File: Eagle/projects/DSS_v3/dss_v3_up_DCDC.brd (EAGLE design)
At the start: 50 x 83 mm, 58 parts, among them IC1 MC34063AD, IC2 Atmega8a, IC3 TL431, J1 12-24V, SW1 EC12E_SW, T1 BC846, X1 PS2

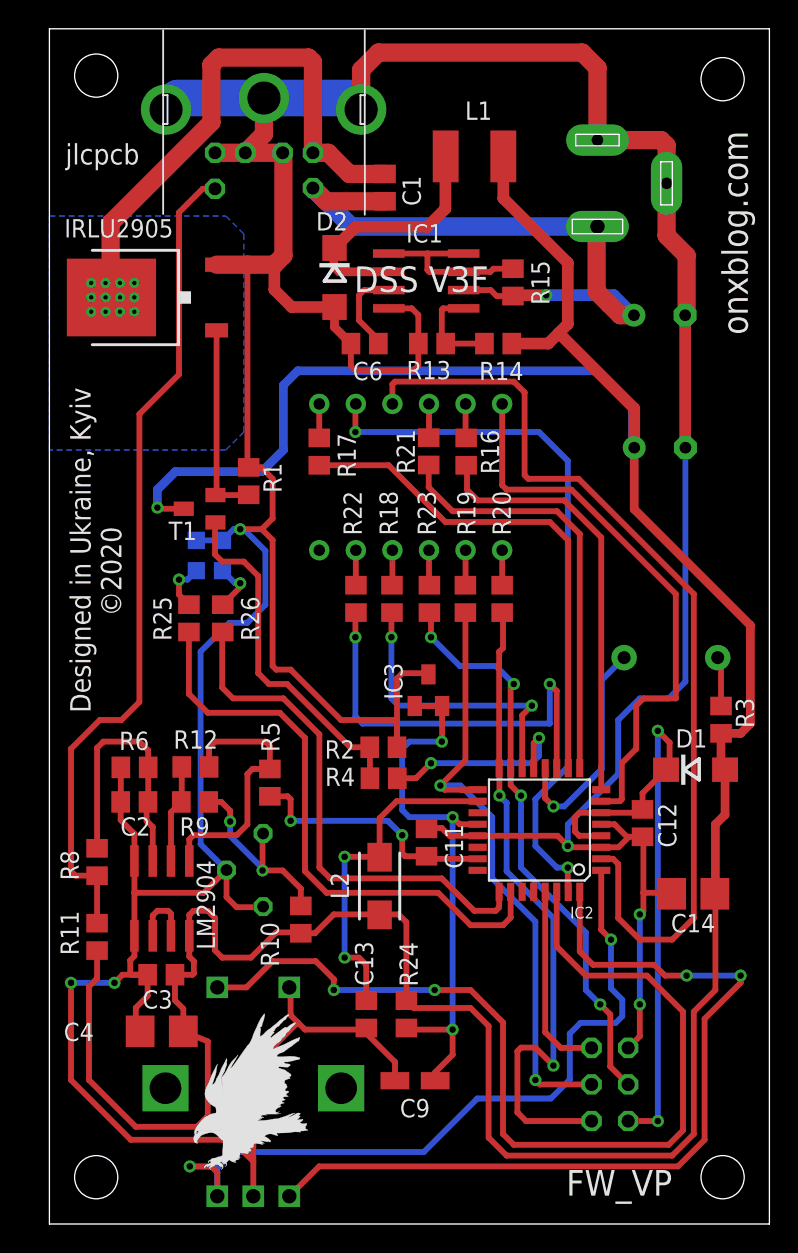
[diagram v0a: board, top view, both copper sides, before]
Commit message: gnd fix add smd capacitor for select
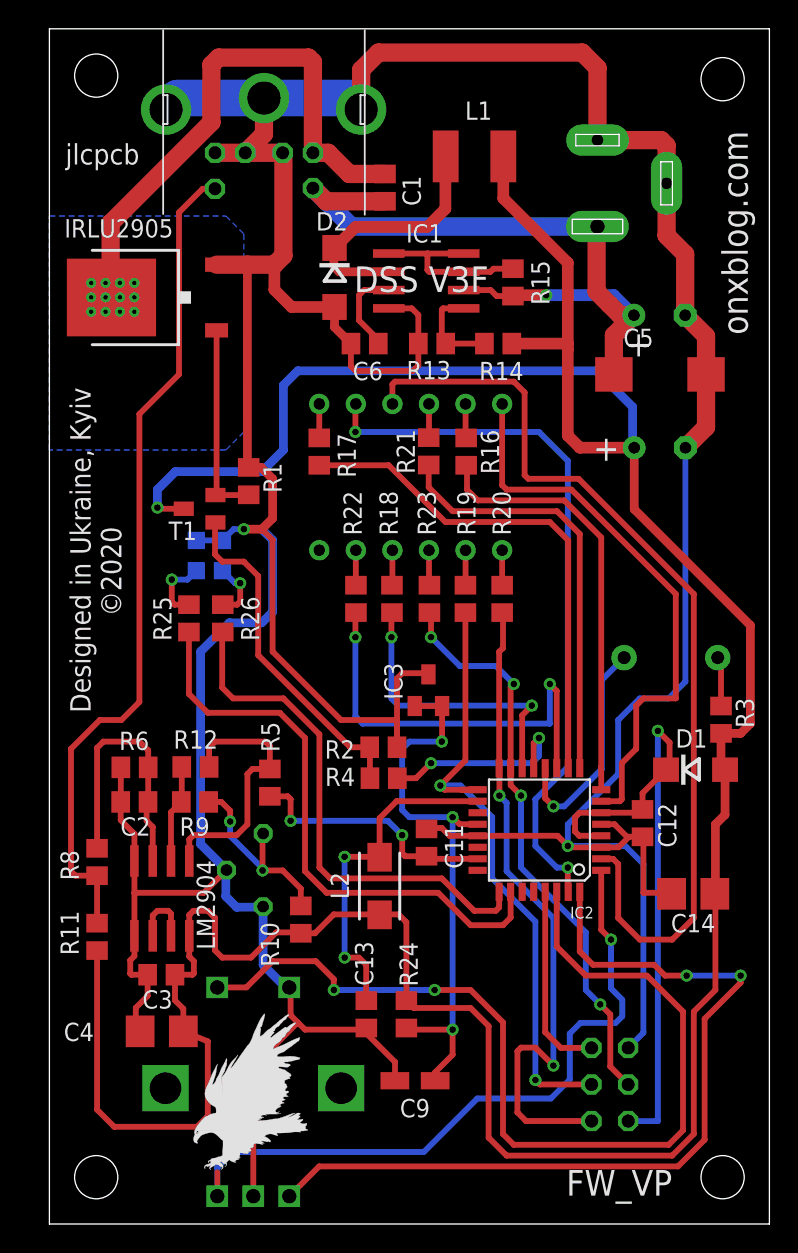
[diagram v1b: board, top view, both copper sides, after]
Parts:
- added C5: 100uF/25v, rcl:CT7343
- C7: value 500u/6.3v -> 1000u/6.3v
- C8: value 100u/35v -> 220u/25v
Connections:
- net GND: now also C5.-
- net HTR+: now also C5.+
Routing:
- net GND: track 343.6 -> 332.6 mm, vias 6 -> 2
- net HTR+: track 47.5 -> 52.2 mm
- net MEGA1: track 52.8 -> 48.7 mm, vias 2 -> 1
- net +5V: track 218.5 -> 220.9 mm
- net N$2: track 3.48 -> 4.78 mm
- net N$13: track 24.6 -> 23.9 mm
- net N$15: track 3.58 -> 4.17 mm
- net P_VCC: vias 2 -> 1
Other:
- board text added: "+"

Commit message: update
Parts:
- C5: device rcl:CT7343 -> rcl:CT6032
- moved C9 27.1 mm to (22.2, 36.9), turned to 90 degrees
- moved R2 5.86 mm to (19.2, 37.4), turned to 270 degrees
- moved R4 1.45 mm to (22.2, 32.0)
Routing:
- net GND: track 332.6 -> 319.3 mm
- net M15_MOSI: track 40.1 -> 46.6 mm
- net HTR+: track 52.2 -> 50.5 mm
- net N$13: track 23.9 -> 22.7 mm

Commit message: update
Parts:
- removed LED3: GREEN, led:CHIP-LED0805
- added LED1: RED, led:CHIP-LED0805
- LED2: value RED -> GREEN
- moved LED2 1.82 mm to (12.0, 46.4)
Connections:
- net GND: now also LED1.C; no longer LED3.C
- net N$15: now also LED2.A; no longer LED3.A
- net N$2: now also LED1.A; no longer LED2.A
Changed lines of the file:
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@@
 <drawing>
 <settings>
-<setting alwaysvectorfont="yes"/>
+<setting alwaysvectorfont="no"/>
 <setting verticaltext="up"/>
 </settings>
@@
 </layers>
 <board>
-<fusionsync huburn="a.cGVyc29uYWw6dWUyZDJlNmQx" projecturn="a.cGVyc29uYWw6dWUyZDJlNmQxIzIwMTgxMTEwMTU5NjEwNjc2" f3durn="urn:adsk.wipprod:dm.lineage:V8w0VrIuR4CtN-5ELGbkjA" pcbguid="e7412862-de73-4a0d-8c51-d66d0301b935" lastpulledtime="" lastsyncedchangeguid="" latestrevisionid="d610ba3a-2b89-4045-b16b-fda7b3353ca0" lastsyncedrevisionid="d610ba3a-2b89-4045-b16b-fda7b3353ca0" lastboardhashguid="1e2e7875-2b4e-3b32-f5dd-e6681731f2c2" lastpushedtime="2020-04-25T01:06:35Z" linktopcb3d="%12"/>
+<fusionsync huburn="a.cGVyc29uYWw6dWUyZDJlNmQx" projecturn="a.cGVyc29uYWw6dWUyZDJlNmQxIzIwMTgxMTEwMTU5NjEwNjc2" f3durn="urn:adsk.wipprod:dm.lineage:V8w0VrIuR4CtN-5ELGbkjA" pcbguid="" lastpulledtime="" lastsyncedchangeguid="" latestrevisionid="74dc081f-416f-463c-a5df-0811a8c10494" lastsyncedrevisionid="74dc081f-416f-463c-a5df-0811a8c10494" lastboardhashguid="81ec6a91-494d-90d3-3657-fe9866165b72" lastpushedtime="2020-05-03T13:46:46Z" linktopcb3d="%12"/>
 <plain>
 <wire x1="0" y1="0" x2="50" y2="0" width="0" layer="20"/>
@@
 <attribute name="VALUE" x="43.41" y="34.742" size="0.6096" layer="28" font="vector" ratio="20" rot="MR180" align="top-center"/>
 </element>
-<element name="C1" library="rcl" package="C0805" value="100nF" x="23.31" y="71.97" smashed="yes" rot="R90">
+<element name="C1" library="rcl" library_urn="urn:adsk.eagle:library:334" package="C0805" package3d_urn="urn:adsk.eagle:package:23617/2" value="100nF" x="23.31" y="71.97" smashed="yes" rot="R90">
 <attribute name="NAME" x="25.79" y="70.7" size="1.27" layer="25" rot="R90"/>
+<attribute name="POPULARITY" value="88" x="23.31" y="71.97" size="1.778" layer="27" rot="R90" display="off"/>
+<attribute name="SPICEPREFIX" value="C" x="23.31" y="71.97" size="1.778" layer="27" rot="R90" display="off"/>
 <attribute name="VALUE" x="25.85" y="70.7" size="1.27" layer="27" rot="R90"/>
 </element>
-<element name="C11" library="rcl" package="C0805" value="100nf" x="26.19" y="26.49" smashed="yes" rot="R270">
+<element name="C11" library="rcl" library_urn="urn:adsk.eagle:library:334" package="C0805" package3d_urn="urn:adsk.eagle:package:23617/2" value="100nf" x="26.19" y="26.49" smashed="yes" rot="R270">
 <attribute name="NAME" x="27.46" y="27.76" size="1.27" layer="25" rot="R270"/>
+<attribute name="POPULARITY" value="88" x="26.19" y="26.49" size="1.778" layer="27" rot="R270" display="off"/>
+<attribute name="SPICEPREFIX" value="C" x="26.19" y="26.49" size="1.778" layer="27" rot="R270" display="off"/>
 <attribute name="VALUE" x="23.65" y="27.76" size="1.27" layer="27" rot="R270"/>
 </element>
-<element name="C12" library="rcl" package="C0805" value="100nf" x="41.19" y="27.84" smashed="yes" rot="R270">
+<element name="C12" library="rcl" library_urn="urn:adsk.eagle:library:334" package="C0805" package3d_urn="urn:adsk.eagle:package:23617/2" value="100nf" x="41.19" y="27.84" smashed="yes" rot="R270">
 <attribute name="NAME" x="43.54" y="26.14" size="1.27" layer="25" rot="R90"/>
+<attribute name="POPULARITY" value="88" x="41.19" y="27.84" size="1.778" layer="27" rot="R270" display="off"/>
+<attribute name="SPICEPREFIX" value="C" x="41.19" y="27.84" size="1.778" layer="27" rot="R270" display="off"/>
 <attribute name="VALUE" x="38.65" y="29.11" size="1.27" layer="27" rot="R270"/>
 </element>
@@
 <attribute name="VALUE" x="33.305" y="47.78" size="1.778" layer="28" ratio="10" rot="MR0"/>
 </element>
-<element name="LED2" library="led" library_urn="urn:adsk.eagle:library:259" package="CHIP-LED0805" package3d_urn="urn:adsk.eagle:package:15818/2" value="RED" x="10.2" y="46.42" smashed="yes" rot="MR0">
+<element name="LED1" library="led" library_urn="urn:adsk.eagle:library:259" package="CHIP-LED0805" package3d_urn="urn:adsk.eagle:package:15818/2" value="RED" x="10.2" y="46.42" smashed="yes" rot="MR0">
 <attribute name="NAME" x="9.72" y="48.4" size="1.27" layer="26" rot="MR90"/>
 <attribute name="POPULARITY" value="68" x="-8.85" y="-31.05" size="1.778" layer="28" rot="MR0" display="off"/>
 <attribute name="VALUE" x="7.66" y="45.15" size="1.27" layer="28" rot="MR90"/>
 </element>
-<element name="LED3" library="led" library_urn="urn:adsk.eagle:library:259" package="CHIP-LED0805" package3d_urn="urn:adsk.eagle:package:15818/2" value="GREEN" x="12.02" y="46.42" smashed="yes" rot="MR0">
+<element name="LED2" library="led" library_urn="urn:adsk.eagle:library:259" package="CHIP-LED0805" package3d_urn="urn:adsk.eagle:package:15818/2" value="GREEN" x="12.02" y="46.42" smashed="yes" rot="MR0">
 <attribute name="NAME" x="11.79" y="48.4" size="1.27" layer="26" rot="MR90"/>
 <attribute name="POPULARITY" value="68" x="-12.11" y="-31.05" size="1.778" layer="28" rot="MR0" display="off"/>
@@
 <contactref element="SW1" pad="C"/>
 <contactref element="SW1" pad="D"/>
+<contactref element="LED1" pad="C"/>
 <contactref element="LED2" pad="C"/>
-<contactref element="LED3" pad="C"/>
 <wire x1="8.1" y1="77.39" x2="8.9" y2="78.19" width="2.54" layer="16"/>
 <wire x1="8.9" y1="78.19" x2="14.9" y2="78.19" width="2.54" layer="16"/>
@@
 <via x="2.9" y="64.35" extent="1-16" drill="0.3"/>
 <via x="2.9" y="65.35" extent="1-16" drill="0.3"/>
-<wire x1="3.9" y1="64.35" x2="4.31" y2="64.34" width="0" layer="19" extent="1-1"/>
+<wire x1="5.9" y1="64.35" x2="5.9" y2="65.35" width="0" layer="19" extent="1-1"/>
+<wire x1="5.9" y1="63.35" x2="5.9" y2="64.35" width="0" layer="19" extent="1-1"/>
+<wire x1="4.9" y1="65.35" x2="5.9" y2="65.35" width="0" layer="19" extent="1-1"/>
+<wire x1="3.9" y1="65.35" x2="4.9" y2="65.35" width="0" layer="19" extent="1-1"/>
+<wire x1="3.9" y1="64.35" x2="3.9" y2="65.35" width="0" layer="19" extent="1-1"/>
+<wire x1="4.31" y1="64.34" x2="3.9" y2="64.35" width="0" layer="19" extent="1-1"/>
+<wire x1="4.9" y1="64.35" x2="4.31" y2="64.34" width="0" layer="19" extent="1-1"/>
+<wire x1="2.9" y1="64.35" x2="3.9" y2="64.35" width="0" layer="19" extent="1-1"/>
+<wire x1="2.9" y1="65.35" x2="3.9" y2="65.35" width="0" layer="19" extent="1-1"/>
+<wire x1="4.9" y1="63.35" x2="5.9" y2="63.35" width="0" layer="19" extent="1-1"/>
+<wire x1="3.9" y1="63.35" x2="3.9" y2="64.35" width="0" layer="19" extent="1-1"/>
+<wire x1="2.9" y1="63.35" x2="2.9" y2="64.35" width="0" layer="19" extent="1-1"/>
 </signal>
 <signal name="N$5">
@@
 <signal name="N$2">
 <contactref element="R25" pad="1"/>
-<contactref element="LED2" pad="A"/>
+<contactref element="LED1" pad="A"/>
 <via x="8.5" y="44.75" extent="1-16" drill="0.45"/>
 <wire x1="10.2" y1="45.37" x2="9.58" y2="44.75" width="0.4064" layer="16"/>
@@
 <signal name="N$15">
 <contactref element="R26" pad="1"/>
-<contactref element="LED3" pad="A"/>
+<contactref element="LED2" pad="A"/>
 <via x="13.25" y="44.5" extent="1-16" drill="0.45"/>
 <wire x1="12.02" y1="45.37" x2="12.89" y2="44.5" width="0.4064" layer="16"/>

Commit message: update
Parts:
- removed U$1: (no value), logo:EAGLE-PLC-8MM
- added U$2: (no value), onx_logo:ONX
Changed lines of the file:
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@@
 <drawing>
 <settings>
-<setting alwaysvectorfont="no"/>
+<setting alwaysvectorfont="yes"/>
 <setting verticaltext="up"/>
 </settings>
@@
 <layer number="59" name="tCarbon" color="7" fill="1" visible="no" active="no"/>
 <layer number="60" name="bCarbon" color="7" fill="1" visible="no" active="no"/>
+<layer number="88" name="SimResults" color="9" fill="1" visible="no" active="no"/>
+<layer number="89" name="SimProbes" color="9" fill="1" visible="no" active="no"/>
 <layer number="90" name="Modules" color="5" fill="1" visible="no" active="no"/>
 <layer number="91" name="Nets" color="2" fill="1" visible="no" active="no"/>
@@
 </layers>
 <board>
-<fusionsync huburn="a.cGVyc29uYWw6dWUyZDJlNmQx" projecturn="a.cGVyc29uYWw6dWUyZDJlNmQxIzIwMTgxMTEwMTU5NjEwNjc2" f3durn="urn:adsk.wipprod:dm.lineage:V8w0VrIuR4CtN-5ELGbkjA" pcbguid="" lastpulledtime="" lastsyncedchangeguid="" latestrevisionid="74dc081f-416f-463c-a5df-0811a8c10494" lastsyncedrevisionid="74dc081f-416f-463c-a5df-0811a8c10494" lastboardhashguid="81ec6a91-494d-90d3-3657-fe9866165b72" lastpushedtime="2020-05-03T13:46:46Z" linktopcb3d="%12"/>
 <plain>
 <wire x1="0" y1="0" x2="50" y2="0" width="0" layer="20"/>
@@
 <text x="48.5" y="61.75" size="1.778" layer="21" rot="R90">onxblog.com</text>
 <text x="30.5" y="66.5" size="1.778" layer="21" rot="R180">DSS V3F</text>
-<text x="43.25" y="3.75" size="1.778" layer="21" rot="R180">FW_VP</text>
+<text x="43.25" y="3" size="1.778" layer="21" rot="R180">FW_VP</text>
 <text x="5" y="35.5" size="1.4224" layer="21" rot="R90">Designed in Ukraine, Kyiv
             ©2020</text>
@@
 <attribute name="VALUE" x="21.25" y="80.73" size="1.778" layer="28" ratio="10" rot="MR0"/>
 </element>
-<element name="U$1" library="logo" library_urn="urn:adsk.eagle:library:264" package="EAGLE-PLC-8MM" value="" x="10" y="3.75" smashed="yes"/>
 <element name="U$3" library="logo" library_urn="urn:adsk.eagle:library:264" package="EAGLE-PLC-8MM" value="" x="12.25" y="30.25" smashed="yes" rot="MR0"/>
 <element name="C5" library="rcl" library_urn="urn:adsk.eagle:library:334" package="CT6032" package3d_urn="urn:adsk.eagle:package:23305/2" value="100uF/25v" x="42.4" y="59" smashed="yes">
@@
 <attribute name="VALUE" x="39.86" y="55.825" size="1.27" layer="27"/>
 </element>
+<element name="U$2" library="onx_logo" package="ONX" value="" x="34.5" y="44.25" smashed="yes"/>
 </elements>
 <signals>
@@
 </note>
 <note version="8.3" severity="warning">
-Since Version 8.3, EAGLE supports Fusion synchronisation.
-This feature will not be available in this version and saving
-the document will break the link to the Fusion PCB feature.
-</note>
-<note version="8.3" severity="warning">

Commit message: update
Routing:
- net MEGA1: track 48.7 -> 46.9 mm
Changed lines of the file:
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@@
 <drawing>
 <settings>
-<setting alwaysvectorfont="yes"/>
+<setting alwaysvectorfont="no"/>
 <setting verticaltext="up"/>
 </settings>
@@
 <wire x1="36.1338" y1="13.2224875" x2="36.8775125" y2="13.9662" width="0.4064" layer="16"/>
 <wire x1="39" y1="16.3584625" x2="39" y2="19.75" width="0.4064" layer="16"/>
-<wire x1="29.7162" y1="8.7162" x2="34.8246625" y2="8.7162" width="0.4064" layer="16"/>
 <wire x1="36.8775125" y1="13.9662" x2="39.3246625" y2="13.9662" width="0.4064" layer="16"/>
 <wire x1="39.7838" y1="15.5746625" x2="39" y2="16.3584625" width="0.4064" layer="16"/>
-<wire x1="34.8246625" y1="8.7162" x2="36.1338" y2="10.0253375" width="0.4064" layer="16"/>
-<wire x1="36.1338" y1="10.0253375" x2="36.1338" y2="13.2224875" width="0.4064" layer="16"/>
+<wire x1="36.1338" y1="10.2753375" x2="36.1338" y2="13.2224875" width="0.4064" layer="16"/>
 <wire x1="38.3226" y1="24.56" x2="38.3226" y2="20.4274" width="0.4064" layer="1"/>
 <wire x1="38.3226" y1="20.4274" x2="39" y2="19.75" width="0.4064" layer="1"/>
 <wire x1="11.66" y1="1.93" x2="11.66" y2="3.91" width="0.4064" layer="16"/>
-<wire x1="26" y1="5" x2="29.7162" y2="8.7162" width="0.4064" layer="16"/>
+<wire x1="30.8584625" y1="5" x2="36.1338" y2="10.2753375" width="0.4064" layer="16"/>
 <wire x1="11.66" y1="3.91" x2="12.75" y2="5" width="0.4064" layer="16"/>
-<wire x1="12.75" y1="5" x2="26" y2="5" width="0.4064" layer="16"/>
-<wire x1="11.66" y1="1.93" x2="11.66" y2="3.59" width="0.4064" layer="1"/>
+<wire x1="12.75" y1="5" x2="30.8584625" y2="5" width="0.4064" layer="16"/>
 </signal>
 <signal name="M15_MOSI">
@@
 </signals>
 <mfgpreviewcolors>
-<mfgpreviewcolor name="soldermaskcolor" color="0xC80C6180"/>
+<mfgpreviewcolor name="soldermaskcolor" color="0xC8214264"/>
 <mfgpreviewcolor name="silkscreencolor" color="0xFFFEFEFE"/>
 <mfgpreviewcolor name="backgroundcolor" color="0xFF282828"/>
-<mfgpreviewcolor name="coppercolor" color="0xFFFFBF00"/>
+<mfgpreviewcolor name="coppercolor" color="0xFFF1F1F1"/>
 <mfgpreviewcolor name="substratecolor" color="0xFF786E46"/>
 </mfgpreviewcolors>

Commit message: update
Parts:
- SW1: device switch-alps:ALPS_EC12E_SW -> switch-alps_3D:ALPS_EC12E_SW
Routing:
- net TSIN+: track 58.2 -> 59.8 mm
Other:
- board text added: "060520"
- board text added: "G R"

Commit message: update
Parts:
- added ON-OFF_HEAT: (no value), jumper:JP1
- moved R4 0.82 mm to (21.5, 32.5), turned to 0 degrees
- moved C9 0.10 mm to (22.2, 37.0)
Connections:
- new net N$17: ON-OFF_HEAT.2, R4.1
- net SH: now also ON-OFF_HEAT.1; no longer R4.1
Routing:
- net N$17: track 0.00 -> 3.03 mm
- net SH: track 14.6 -> 15.9 mm
- net N$13: track 22.7 -> 23.7 mm
- net N$23: track 23.6 -> 22.9 mm
